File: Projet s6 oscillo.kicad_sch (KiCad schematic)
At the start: 11 parts, among them IC1 PGA849RGTR, J1 Conn_Coaxial, U1 STM32L476RGTx

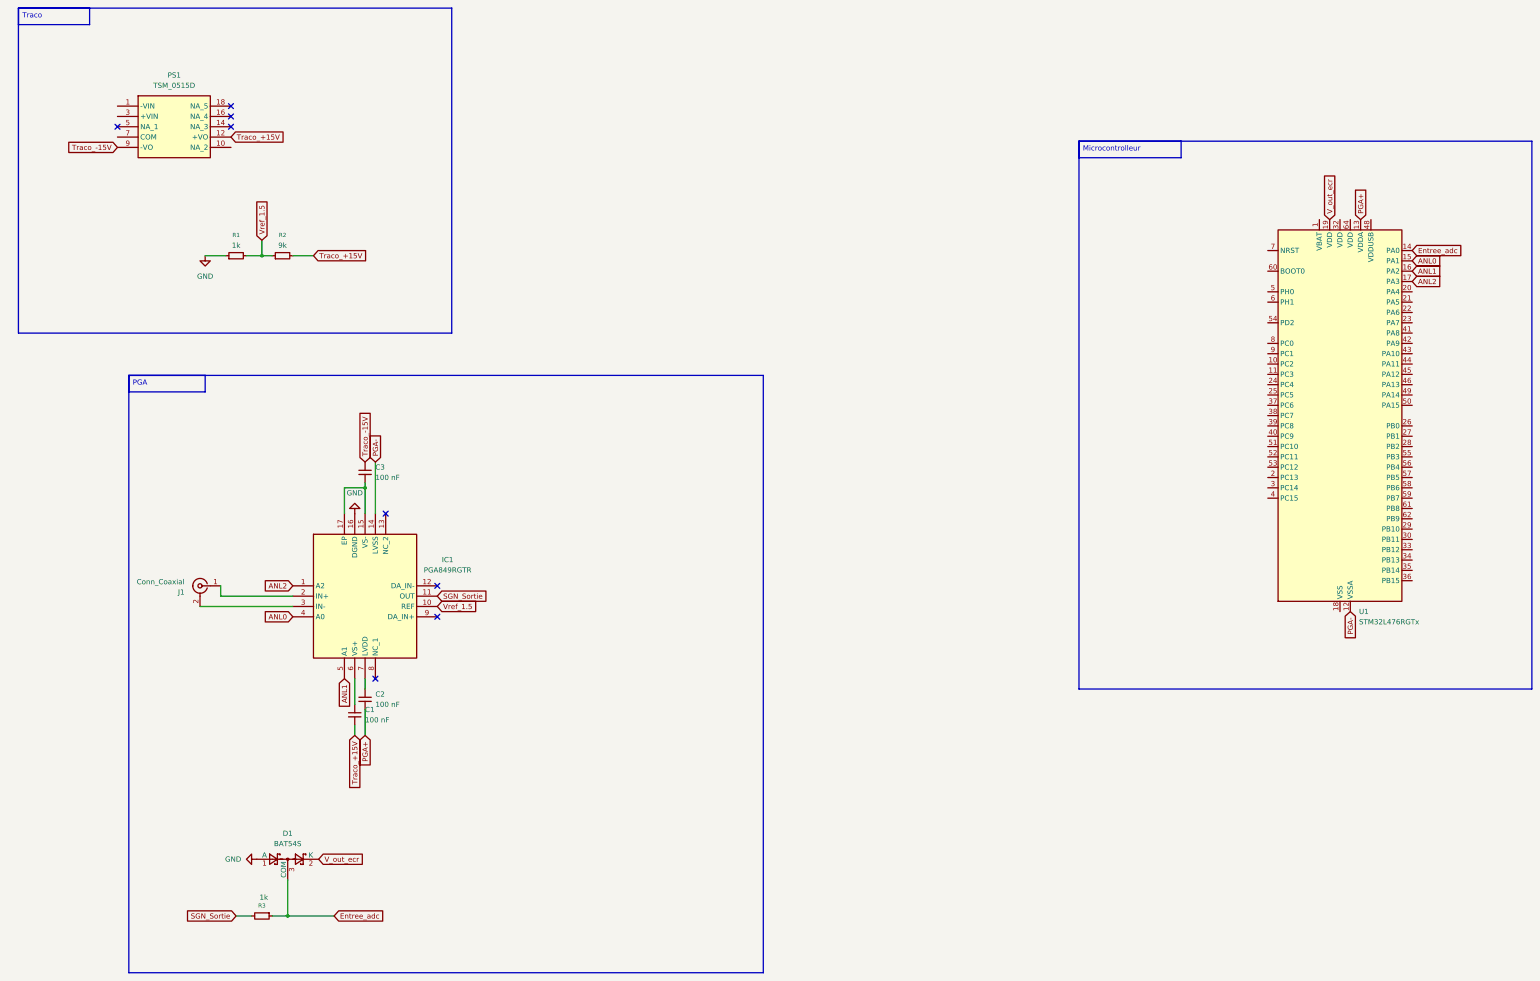
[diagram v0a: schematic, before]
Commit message: schematic adc v2
pin for HC05, improvment of pont diviseur
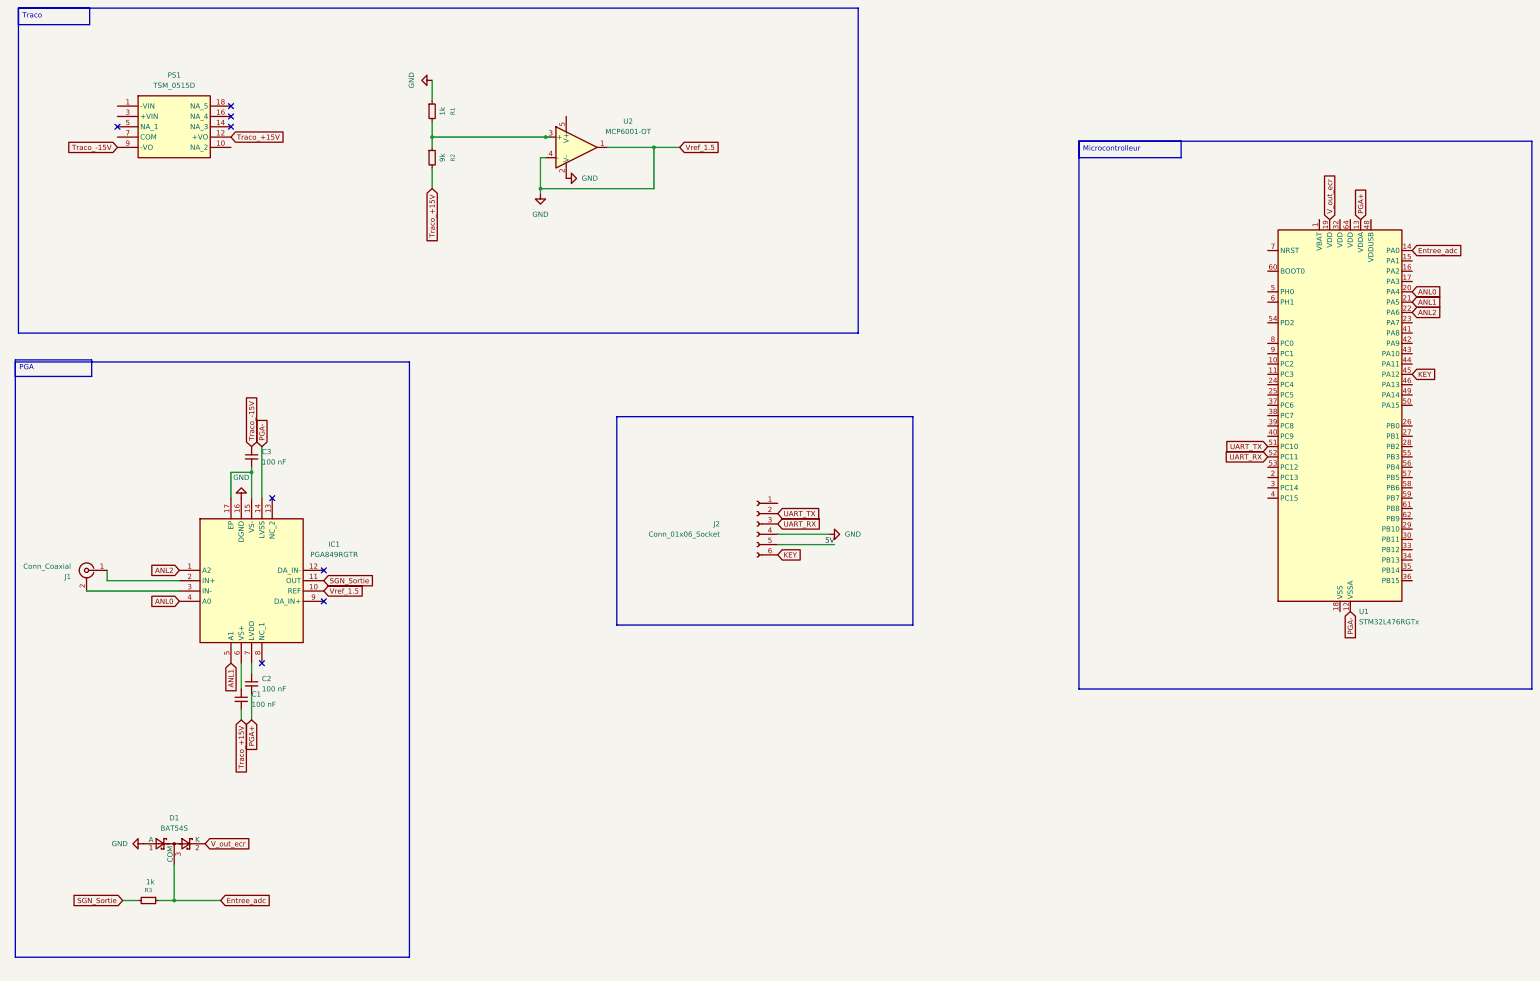
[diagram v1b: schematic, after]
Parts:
- added J2: Conn_01x06_Socket, Connector_Harwin:Harwin_M20-89006xx_1x06_P2.54mm_Horizontal, symbol Connector:Conn_01x06_Socket
- added U2: MCP6001-OT, Package_TO_SOT_SMD:SOT-23-5, symbol Amplifier_Operational:MCP6001-OT
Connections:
- net ANL0: now also U1.20 (PA4); no longer U1.15 (PA1)
- net ANL1: now also U1.21 (PA5); no longer U1.16 (PA2)
- net ANL2: now also U1.22 (PA6); no longer U1.17 (PA3)
- net GND: now also IC1.10 (REF), J2.4 (Pin_4), U2.1, U2.2 (V-), U2.4 (-)
- net KEY: now reaches U1.45 (PA12)
- net KEY: now also J2.6 (Pin_6)
- net UART_TX: now reaches U1.51 (PC10)
- net UART_TX: now also J2.2 (Pin_2)
- net UART_RX: now reaches U1.52 (PC11)
- net UART_RX: now also J2.3 (Pin_3)
- net Vref_1.5: no longer names the net of R1.2, R2.1
- net Vref_1.5: now also U2.3 (+); no longer IC1.10 (REF)
- new net 5V: J2.5 (Pin_5)
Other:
- moved on the sheet: C1, C2, C3, D1, IC1, J1, R1, R2, R3

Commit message: v4
Addition of zener instead of op amp for generating 1.5V
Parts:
- removed R2: 9k, symbol Device:R_Small
- removed U2: MCP6001-OT, Package_TO_SOT_SMD:SOT-23-5, symbol Amplifier_Operational:MCP6001-OT
- added C4: 4.7µ, symbol Device:C
- added D2: D_Zener, symbol Device:D_Zener
- added J3: PILES_3AA, symbol Connector_Generic:Conn_01x02
- added R4: 1k, symbol Device:R
- added R5: 300, symbol Device:R
- added SW1: SW_SPST, symbol Switch:SW_SPST
- added U3: AP2112K-3.3, Package_TO_SOT_SMD:SOT-23-5, symbol Regulator_Linear:AP2112K-3.3
- added U3: MCP1640x-xCHY, Package_TO_SOT_SMD:SOT-23-6, symbol Regulator_Switching:MCP1640x-xCHY
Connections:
- net GND: now also R1.2, C4.2, J3.2 (Pin_2), R5.2, U3.2 (GND), U3.2 (GND); no longer IC1.10 (REF), R1.1
- net Traco_+15V: now also IC1.10 (REF), D2.2 (A)
- net +3.3V: now reaches U1.32 (VDD)
- net +3.3V: now also U3.5 (VOUT)
- new net: D2.1 (K), R1.1
- new net: R4.1, R5.1, U3.4 (V_{FB})
- new net BAT_PLUS: J3.1 (Pin_1), SW1.1 (A)
- new net Sortie5V_BOOST: R4.2, U3.5 (V_{OUT})
- new net switch_Out: C4.1, SW1.2 (B), U3.1 (VIN), U3.3 (EN), U3.3 (EN), U3.6 (V_{IN})
